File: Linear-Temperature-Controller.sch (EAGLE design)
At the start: 1 part

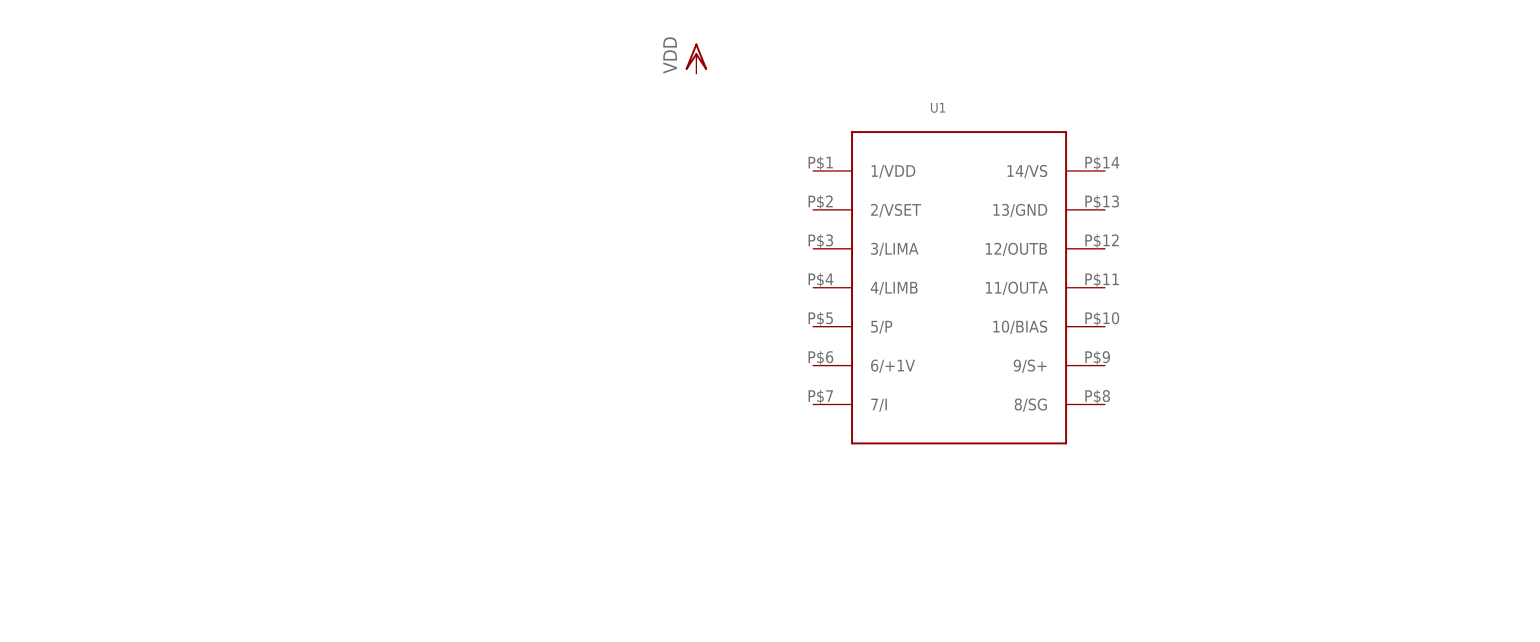
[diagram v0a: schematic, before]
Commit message: Added current limit portion
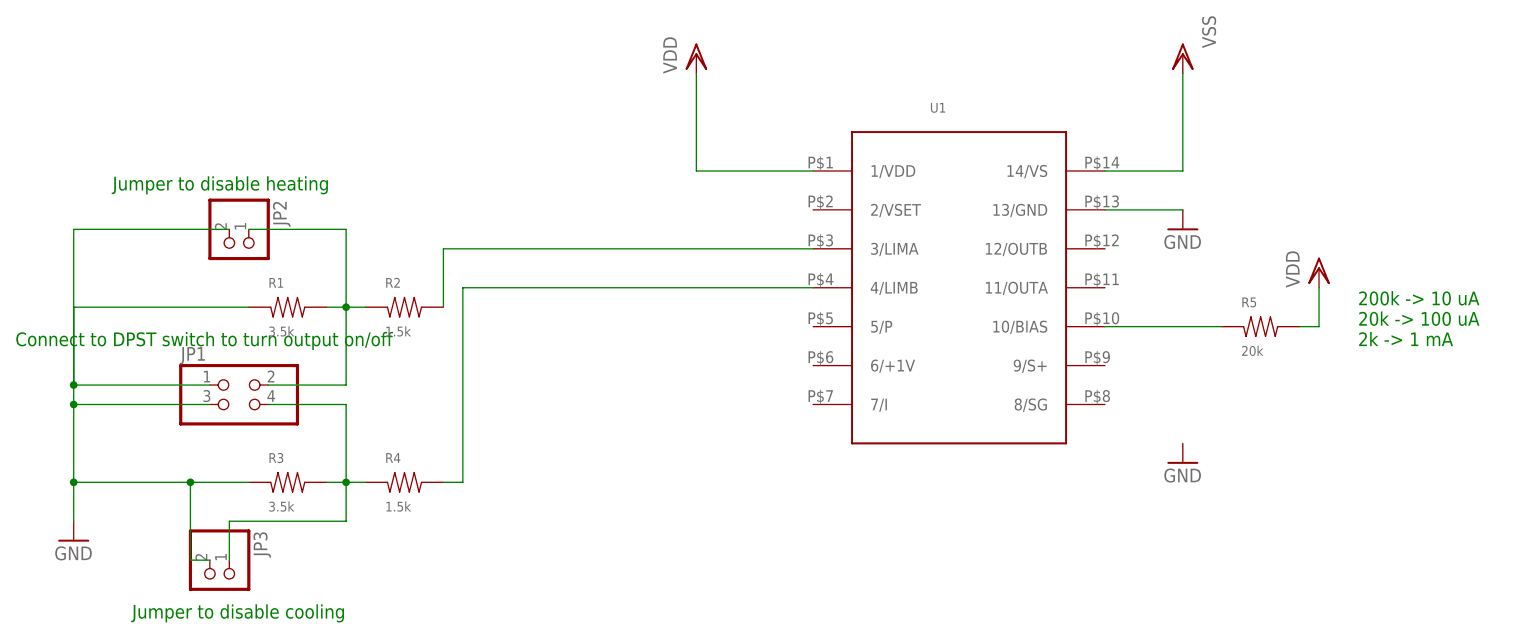
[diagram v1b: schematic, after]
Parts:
- added JP1: (no value), pinhead:PINHD-2X2
- added JP2, JP3: (no value), pinhead:PINHD-1X2
- added R1, R3: 3.5k, rlc-jqi:RES0805
- added R2, R4: 1.5k, rlc-jqi:RES0805
- added R5: 20k, rlc-jqi:RES0805
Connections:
- new net GND: JP1.1, JP1.3, JP2.2, JP3.2, R1.P$1, R3.P$1, U1.13/GND
- new net N$1: R2.P$2, U1.3/LIMA
- new net N$2: JP1.2, JP2.1, R1.P$2, R2.P$1
- new net N$3: R4.P$2, U1.4/LIMB
- new net N$4: JP1.4, JP3.1, R3.P$2, R4.P$1
- new net N$5: R5.P$1, U1.10/BIAS
- new net VDD: R5.P$2, U1.1/VDD
- new net VSS: U1.14/VS
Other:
- note added: "200k -> 10 uA 20k -> 100 uA 2k -> 1 mA"
- note added: "Connect to DPST switch to turn output on/off"
- note added: "Jumper to disable cooling"
- note added: "Jumper to disable heating"
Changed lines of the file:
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@@
 <part name="U1" library="Lin-Temp-Controller" deviceset="WTC3243" device=""/>
 <part name="VDD1" library="supply1" deviceset="VDD" device=""/>
+<part name="R1" library="rlc-jqi" deviceset="RES" device="0805" value="3.5k"/>
+<part name="R2" library="rlc-jqi" deviceset="RES" device="0805" value="1.5k"/>
+<part name="JP1" library="pinhead" deviceset="PINHD-2X2" device=""/>
+<part name="JP2" library="pinhead" deviceset="PINHD-1X2" device=""/>
+<part name="JP3" library="pinhead" deviceset="PINHD-1X2" device=""/>
+<part name="R3" library="rlc-jqi" deviceset="RES" device="0805" value="3.5k"/>
+<part name="R4" library="rlc-jqi" deviceset="RES" device="0805" value="1.5k"/>
+<part name="GND1" library="supply1" deviceset="GND" device=""/>
+<part name="GND2" library="supply1" deviceset="GND" device=""/>
+<part name="GND3" library="supply1" deviceset="GND" device=""/>
+<part name="VSS1" library="supply1" deviceset="VSS" device=""/>
+<part name="R5" library="rlc-jqi" deviceset="RES" device="0805" value="20k"/>
+<part name="VDD2" library="supply1" deviceset="VDD" device=""/>
 </parts>
 <sheets>
 <sheet>
 <plain>
+<text x="-50.8" y="45.72" size="1.778" layer="91">Jumper to disable heating</text>
+<text x="-48.26" y="-10.16" size="1.778" layer="91">Jumper to disable cooling</text>
+<text x="-63.5" y="25.4" size="1.778" layer="91">Connect to DPST switch to turn output on/off</text>
+<text x="111.76" y="25.4" size="1.778" layer="91">200k -&gt; 10 uA
+20k -&gt; 100 uA
+2k -&gt; 1 mA</text>
 </plain>
 <instances>
 <instance part="U1" gate="G$1" x="58.42" y="35.56"/>
 <instance part="VDD1" gate="G$1" x="25.4" y="63.5"/>
+<instance part="R1" gate="G$1" x="-27.94" y="30.48"/>
+<instance part="R2" gate="G$1" x="-12.7" y="30.48"/>
+<instance part="JP1" gate="A" x="-33.02" y="17.78"/>
+<instance part="JP2" gate="G$1" x="-35.56" y="38.1" rot="R270"/>
+<instance part="JP3" gate="G$1" x="-38.1" y="-5.08" rot="R270"/>
+<instance part="R3" gate="G$1" x="-27.94" y="7.62"/>
+<instance part="R4" gate="G$1" x="-12.7" y="7.62"/>
+<instance part="GND1" gate="1" x="-55.88" y="0"/>
+<instance part="GND2" gate="1" x="88.9" y="40.64"/>
+<instance part="GND3" gate="1" x="88.9" y="10.16"/>
+<instance part="VSS1" gate="G$1" x="88.9" y="63.5" rot="R180"/>
+<instance part="R5" gate="G$1" x="99.06" y="27.94"/>
+<instance part="VDD2" gate="G$1" x="106.68" y="35.56"/>
 </instances>
 <busses>
 </busses>
 <nets>
+<net name="N$1" class="0">
+<segment>
+<pinref part="U1" gate="G$1" pin="3/LIMA"/>
+<pinref part="R2" gate="G$1" pin="P$2"/>
+<wire x1="40.64" y1="38.1" x2="-7.62" y2="38.1" width="0.1524" layer="91"/>
+<wire x1="-7.62" y1="38.1" x2="-7.62" y2="30.48" width="0.1524" layer="91"/>
+</segment>
+</net>
+<net name="N$2" class="0">
+<segment>
+<pinref part="R2" gate="G$1" pin="P$1"/>
+<wire x1="-17.78" y1="30.48" x2="-20.32" y2="30.48" width="0.1524" layer="91"/>
+<wire x1="-20.32" y1="30.48" x2="-20.32" y2="20.32" width="0.1524" layer="91"/>
+<pinref part="JP1" gate="A" pin="2"/>
+<wire x1="-20.32" y1="20.32" x2="-30.48" y2="20.32" width="0.1524" layer="91"/>
+<junction x="-20.32" y="30.48"/>
+<pinref part="R1" gate="G$1" pin="P$2"/>
+<wire x1="-22.86" y1="30.48" x2="-20.32" y2="30.48" width="0.1524" layer="91"/>
+<wire x1="-20.32" y1="30.48" x2="-20.32" y2="40.64" width="0.1524" layer="91"/>
+<pinref part="JP2" gate="G$1" pin="1"/>
+<wire x1="-20.32" y1="40.64" x2="-33.02" y2="40.64" width="0.1524" layer="91"/>
+</segment>
+</net>
+<net name="GND" class="0">
+<segment>
+<pinref part="R1" gate="G$1" pin="P$1"/>
+<pinref part="GND1" gate="1" pin="GND"/>
+<wire x1="-33.02" y1="30.48" x2="-55.88" y2="30.48" width="0.1524" layer="91"/>
+<wire x1="-55.88" y1="30.48" x2="-55.88" y2="20.32" width="0.1524" layer="91"/>
+<pinref part="R3" gate="G$1" pin="P$1"/>
+<wire x1="-55.88" y1="20.32" x2="-55.88" y2="17.78" width="0.1524" layer="91"/>
+<wire x1="-55.88" y1="17.78" x2="-55.88" y2="7.62" width="0.1524" layer="91"/>
+<wire x1="-55.88" y1="7.62" x2="-55.88" y2="2.54" width="0.1524" layer="91"/>
+<wire x1="-33.02" y1="7.62" x2="-40.64" y2="7.62" width="0.1524" layer="91"/>
+<junction x="-55.88" y="7.62"/>
+<junction x="-55.88" y="20.32"/>
+<junction x="-55.88" y="17.78"/>
+<pinref part="JP2" gate="G$1" pin="2"/>
+<wire x1="-40.64" y1="7.62" x2="-55.88" y2="7.62" width="0.1524" layer="91"/>
+<wire x1="-35.56" y1="40.64" x2="-55.88" y2="40.64" width="0.1524" layer="91"/>
+<wire x1="-55.88" y1="40.64" x2="-55.88" y2="20.32" width="0.1524" layer="91"/>
+<pinref part="JP1" gate="A" pin="1"/>
+<wire x1="-38.1" y1="20.32" x2="-55.88" y2="20.32" width="0.1524" layer="91"/>
+<pinref part="JP1" gate="A" pin="3"/>
+<wire x1="-38.1" y1="17.78" x2="-55.88" y2="17.78" width="0.1524" layer="91"/>
+<pinref part="JP3" gate="G$1" pin="2"/>
+<wire x1="-38.1" y1="-2.54" x2="-40.64" y2="-2.54" width="0.1524" layer="91"/>
+<wire x1="-40.64" y1="-2.54" x2="-40.64" y2="7.62" width="0.1524" layer="91"/>
+<junction x="-40.64" y="7.62"/>
+</segment>
+<segment>
+<pinref part="GND2" gate="1" pin="GND"/>
+<pinref part="U1" gate="G$1" pin="13/GND"/>
+<wire x1="88.9" y1="43.18" x2="78.74" y2="43.18" width="0.1524" layer="91"/>
+</segment>
+</net>
+<net name="N$3" class="0">
+<segment>
+<pinref part="U1" gate="G$1" pin="4/LIMB"/>
+<wire x1="40.64" y1="33.02" x2="-5.08" y2="33.02" width="0.1524" layer="91"/>
+<wire x1="-5.08" y1="33.02" x2="-5.08" y2="7.62" width="0.1524" layer="91"/>
+<pinref part="R4" gate="G$1" pin="P$2"/>
+<wire x1="-5.08" y1="7.62" x2="-7.62" y2="7.62" width="0.1524" layer="91"/>
+</segment>
+</net>
+<net name="N$4" class="0">
+<segment>
+<pinref part="R4" gate="G$1" pin="P$1"/>
+<pinref part="R3" gate="G$1" pin="P$2"/>
+<wire x1="-17.78" y1="7.62" x2="-20.32" y2="7.62" width="0.1524" layer="91"/>
+<junction x="-20.32" y="7.62"/>
+<wire x1="-20.32" y1="7.62" x2="-22.86" y2="7.62" width="0.1524" layer="91"/>
+<wire x1="-20.32" y1="7.62" x2="-20.32" y2="2.54" width="0.1524" layer="91"/>
+<pinref part="JP3" gate="G$1" pin="1"/>
+<wire x1="-20.32" y1="2.54" x2="-35.56" y2="2.54" width="0.1524" layer="91"/>
+<wire x1="-35.56" y1="2.54" x2="-35.56" y2="-2.54" width="0.1524" layer="91"/>
+<wire x1="-20.32" y1="7.62" x2="-20.32" y2="17.78" width="0.1524" layer="91"/>
+<pinref part="JP1" gate="A" pin="4"/>
+<wire x1="-20.32" y1="17.78" x2="-30.48" y2="17.78" width="0.1524" layer="91"/>
+</segment>
+</net>
+<net name="VDD" class="0">
+<segment>
+<pinref part="U1" gate="G$1" pin="1/VDD"/>
+<pinref part="VDD1" gate="G$1" pin="VDD"/>
+<wire x1="40.64" y1="48.26" x2="25.4" y2="48.26" width="0.1524" layer="91"/>
+<wire x1="25.4" y1="48.26" x2="25.4" y2="60.96" width="0.1524" layer="91"/>
+</segment>
+<segment>
+<pinref part="R5" gate="G$1" pin="P$2"/>
+<pinref part="VDD2" gate="G$1" pin="VDD"/>
+<wire x1="104.14" y1="27.94" x2="106.68" y2="27.94" width="0.1524" layer="91"/>
+<wire x1="106.68" y1="27.94" x2="106.68" y2="33.02" width="0.1524" layer="91"/>
+</segment>
+</net>
+<net name="VSS" class="0">
+<segment>
+<pinref part="VSS1" gate="G$1" pin="VSS"/>
+<wire x1="88.9" y1="60.96" x2="88.9" y2="48.26" width="0.1524" layer="91"/>
+<pinref part="U1" gate="G$1" pin="14/VS"/>
+<wire x1="88.9" y1="48.26" x2="78.74" y2="48.26" width="0.1524" layer="91"/>
+</segment>
+</net>
+<net name="N$5" class="0">
+<segment>
+<pinref part="U1" gate="G$1" pin="10/BIAS"/>
+<pinref part="R5" gate="G$1" pin="P$1"/>
+<wire x1="78.74" y1="27.94" x2="93.98" y2="27.94" width="0.1524" layer="91"/>
+</segment>
+</net>
 </nets>
 </sheet>
@@
 </schematic>
 </drawing>
+<compatibility>
+<note version="6.3" minversion="6.2.2" severity="warning">
+Since Version 6.2.2 text objects can contain more than one line,
+which will not be processed correctly with this version.
+</note>
+</compatibility>
 </eagle>

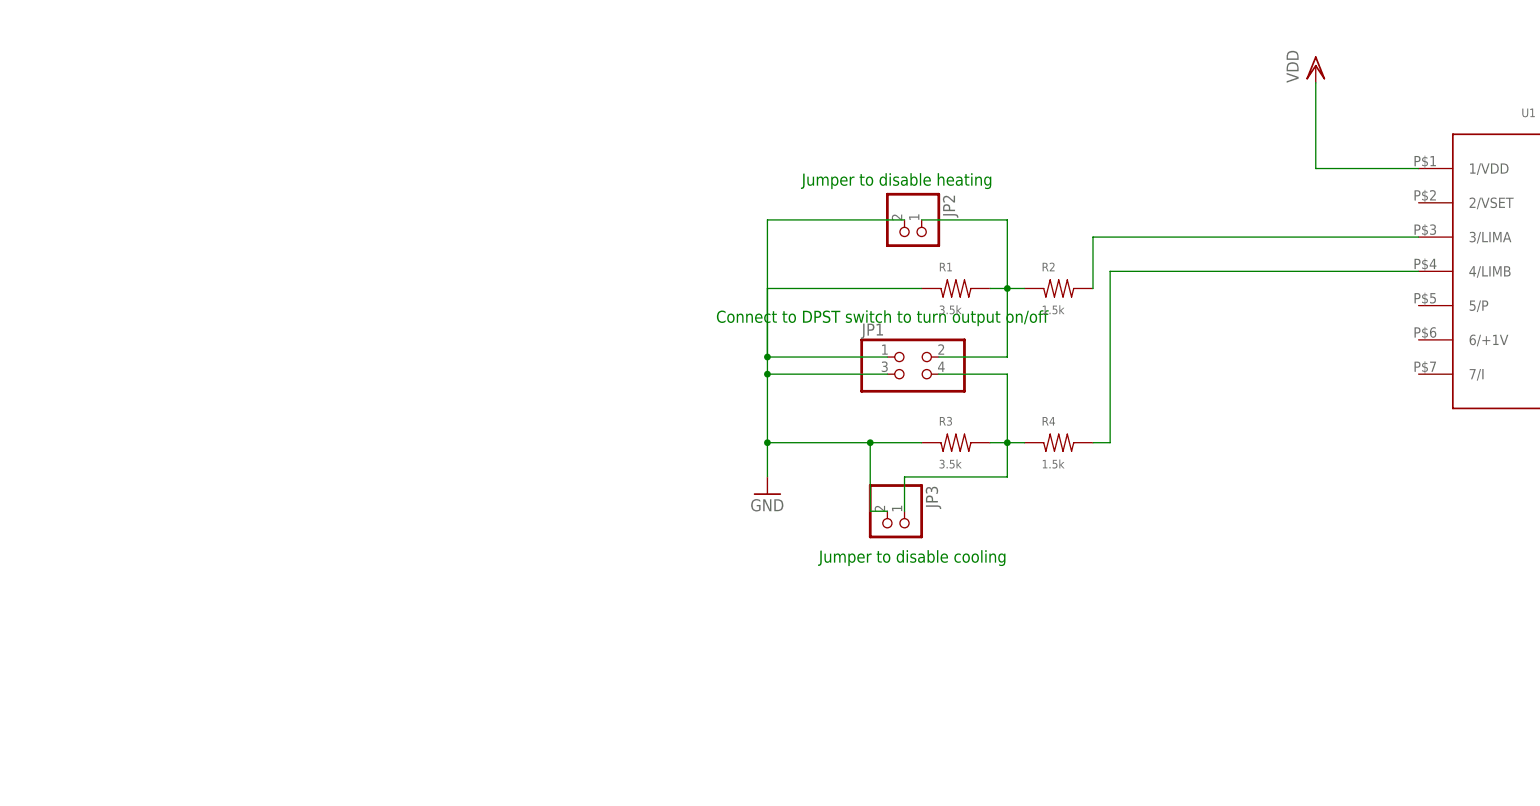
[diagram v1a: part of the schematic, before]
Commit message: Add input voltage protection
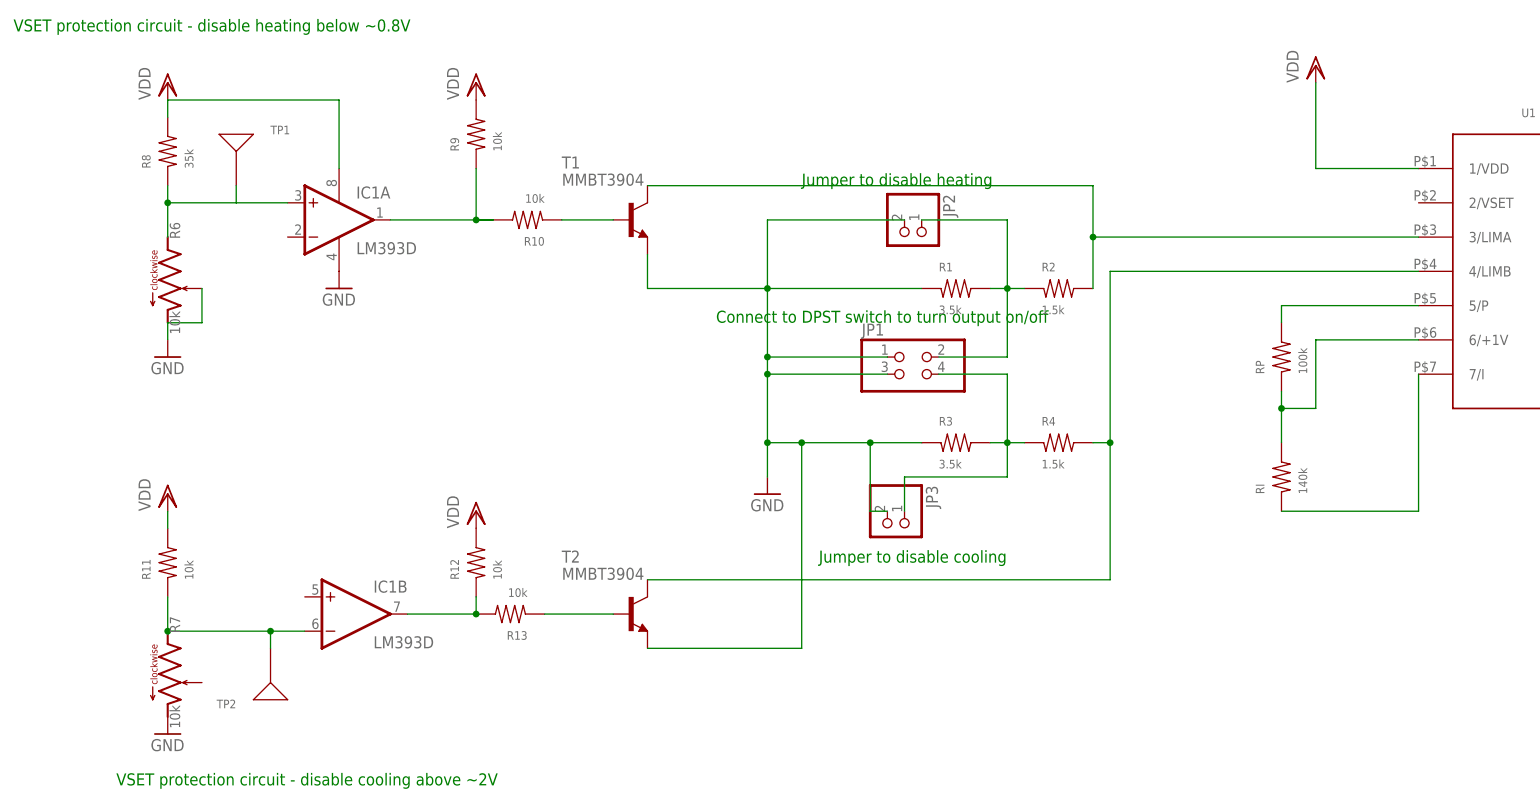
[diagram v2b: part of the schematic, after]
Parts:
- added IC1: LM393D, Lin-Temp-Controller:LM393D
- added R10, R11, R12, R13, R9: 10k, rlc-jqi:RES0805
- added R6, R7: 10k, jqi_passives:R_TRIMPOT_SMD_BOURNS-3224XBOURNS
- added R8: 35k, rlc-jqi:RES0805
- added RI: 140k, rlc-jqi:RES0805
- added RP: 100k, rlc-jqi:RES0805
- added T1, T2: MMBT3904, Lin-Temp-Controller:MMBT3904
- added TP1, TP2: TEST_PAD150, connector-jqi:TEST_PAD150
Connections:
- new net N$10: R10.P$1, T1.B
- new net N$11: R13.P$1, T2.B
- new net N$13: RP.P$2, U1.5/P
- new net N$14: RI.P$2, RP.P$1, U1.6/+1V
- new net N$15: RI.P$1, U1.7/I
- new net N$6: IC1A.+IN, R6.1, R8.P$1, TP1.P$1
- new net N$7: IC1B.-IN, R11.P$1, R7.1, TP2.P$1
- new net N$8: IC1B.OUT, R12.P$1, R13.P$2
- new net N$9: IC1A.OUT, R10.P$2, R9.P$1
- net GND: now also IC1P.V-, R6.2, R6.3, R7.3, T1.E, T2.E
- net N$1: now also T1.C
- net N$3: now also T2.C
- net VDD: now also IC1P.V+, R11.P$2, R12.P$2, R8.P$2, R9.P$2
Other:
- note added: "VSET protection circuit - disable cooling above ~2V"
- note added: "VSET protection circuit - disable heating below ~0.8V"

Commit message: Schematic Progress
Include microcontroller, DAC, digital POT and more
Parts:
- added C1: 10nF, rlc-jqi:CAP0603
- added C2: 10uF, rlc-jqi:CAP0603
- added C27, C3, C4: 100nF, rlc-jqi:CAP0603
- added C30, C5: 10uF, rlc-jqi:CAP0805
- added CP1, CP4: 220uF, rcl:CPOL-USF
- added CP2, CP6: 10uF, rcl:C-USC0805K
- added CP3, CP5: 47uF, rcl:CPOL-USCT7343
- added ENC_HEADER1, LCD_HEADER1: 2x8Header, mcu-accessories:ML16
- added IC2: MEGA8-AI, atmel:MEGA8-AI
- added IC3: AD5624R, Lin-Temp-Controller:AD5624R
- added IC4: AD5262, Lin-Temp-Controller:AD5262
- added JP4, JP5: (no value), pinhead:PINHD-1X2
- added LP1, LP2: SDR1005-101K, misc-ics:SDR1005-101K
- added R14: 10k, rlc-jqi:RES0805
- added R15: 10k, rlc-jqi:RES0603
- added R16, R17: 0, rlc-jqi:RES0805
- added SV2: 2x3Header, con-lstb:MA03-2
- RI: value 140k -> DNP
- RP: value 100k -> DNP
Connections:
- removed net N$13: RP.P$2, U1.5/P
- removed net N$14: RI.P$2, RP.P$1, U1.6/+1V
- new net +5V: CP1.+, CP2.1, JP4.2, LP1.1
- new net A6: IC2.ADC6
- new net A7: IC2.ADC7
- new net CLR: IC2.PD6(AIN0)
- new net CSB: IC2.PC3(ADC3), LCD_HEADER1.5
- new net CS_POT: IC2.PD7(AIN1), IC4.CS
- new net D10: IC2.PB2(SS/OC1B)
- new net D9: IC2.PB1(OC1A)
- new net ENC_A: ENC_HEADER1.7, IC2.PD2(INT0)
- new net ENC_B: ENC_HEADER1.5, IC2.PD3(INT1)
- new net ENC_SW: ENC_HEADER1.1, IC2.PD5(T1)
- new net I2C_SCL: IC2.PC5(ADC5/SCL)
- new net I2C_SDA: IC2.PC4(ADC4/SDA)
- new net MISO: IC2.PB4(MISO), SV2.1
- new net MOSI: IC2.PB3(MOSI/OC2), IC3.DIN, IC4.SDI, LCD_HEADER1.9, SV2.4
- new net N$12: R14.P$1, U1.2/VSET
- new net N$16: C3.P$2, IC2.AREF
- new net N$17: R16.P$2, R17.P$1, RI.P$2, RP.P$1, U1.6/+1V
- new net N$18: IC4.B1, IC4.W1, R16.P$1
- new net N$19: IC4.A2, RI.P$1
- new net N$20: IC4.B2, IC4.W2, R17.P$2
- new net PC0: IC2.PC0(ADC0)
- new net PC1: IC2.PC1(ADC1)
- new net PC2: IC2.PC2(ADC2)
- new net RESET: IC2.PC6(/RESET), R15.P$1, SV2.5
- new net RS: IC2.PD0(RXD), LCD_HEADER1.3
- new net RST: IC2.PD1(TXD), LCD_HEADER1.1
- new net SCK: IC2.PB5(SCK), IC3.SCLK, IC4.CLK, LCD_HEADER1.7, SV2.3
- new net SW1: ENC_HEADER1.3, IC2.PD4(XCK/T0)
- new net SYNC: IC2.PB0(ICP), IC3.SYNC
- new net V+: CP4.+, CP6.1, JP5.2, LP2.1
- new net VSET: IC1A.-IN, IC1B.+IN, IC3.VOUTA, R14.P$2
- net GND: now also C1.P$1, C2.P$1, C27.P$1, C3.P$1, C30.P$1, C4.P$1, C5.P$1, CP1.-, CP2.2, CP3.-, CP4.-, CP5.-, CP6.2, ENC_HEADER1.15, IC2.GND, IC2.GND@1, IC2.GND@2, IC3.GND, IC4.GND, IC4.VSS, JP4.1, JP5.1, LCD_HEADER1.11, SV2.6
- net N$15: now also IC4.A1, RP.P$2, U1.5/P; no longer RI.P$1, U1.7/I
- net VDD: now also C1.P$2, C2.P$2, C27.P$2, C30.P$2, C4.P$2, C5.P$2, CP3.+, ENC_HEADER1.4, IC2.AVCC, IC2.VCC@1, IC2.VCC@2, IC3.VDD, IC4.VDD, IC4.VL, LCD_HEADER1.13, LP1.2, R15.P$2, SV2.2
- net VSS: now also CP5.+, LP2.2
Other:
- note added: "+5V filtered"
- note added: "+V filtered"
- note added: "100uH"
- note added: "Chip select bit"
- note added: "LCD pins"
- note added: "Register select"
- note added: "SPI bus"
- note added: "decouples internal reference"
- note added: "reset"
